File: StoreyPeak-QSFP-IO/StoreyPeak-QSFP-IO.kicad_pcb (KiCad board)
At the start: 2 copper layers, 30.1 x 69.8 mm, 26 parts, among them U1 QSFP_PCB-QSFP, U3 CH340G, X1 X322512MSB4SI

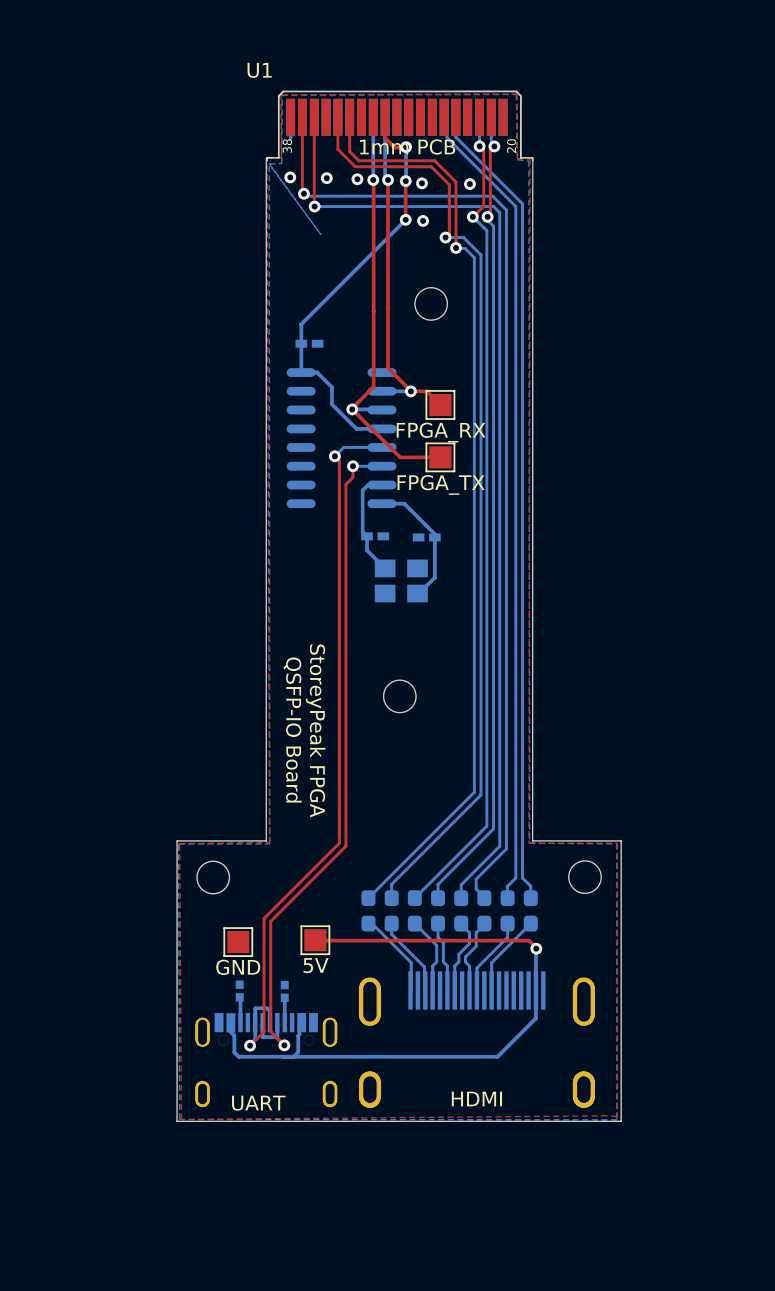
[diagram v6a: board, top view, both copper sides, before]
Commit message: Fix board outline cuts
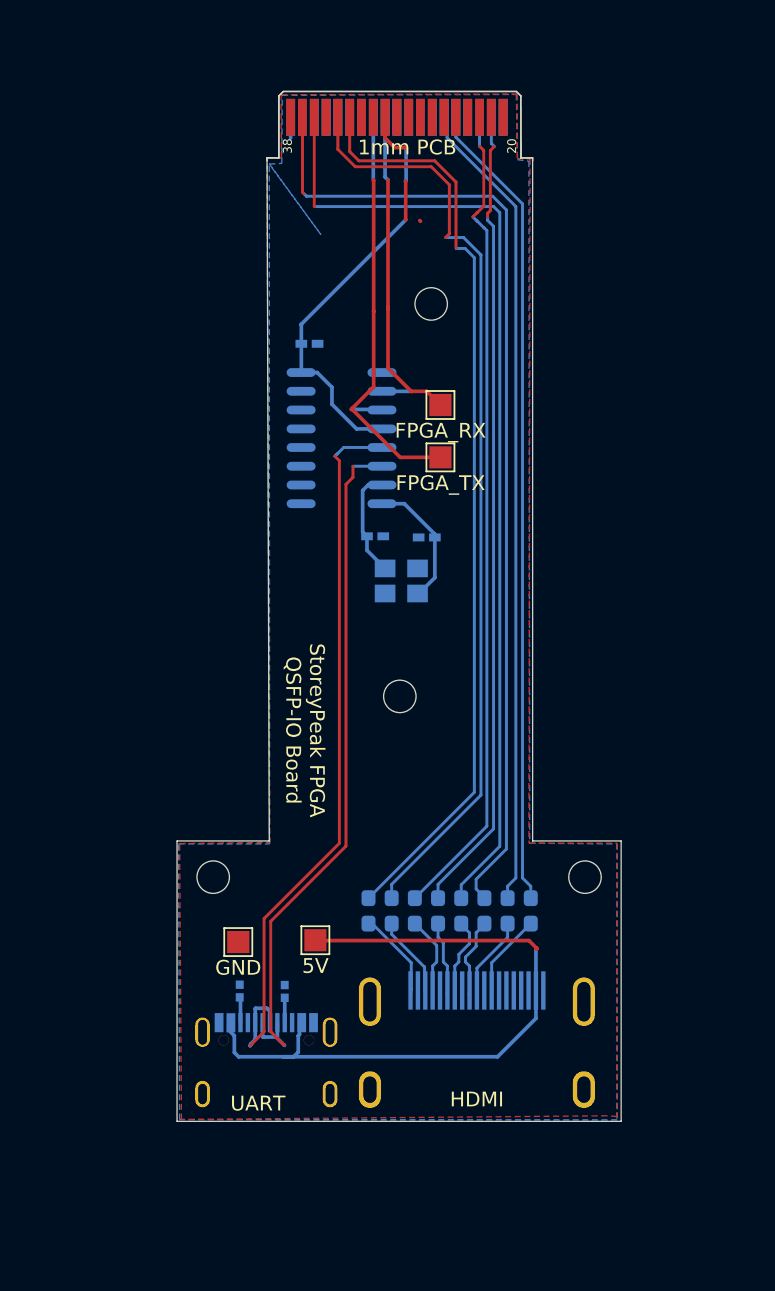
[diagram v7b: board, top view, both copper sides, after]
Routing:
- net Net-(U1-SDA): vias 2 -> 0
- net Net-(U1-SCL): vias 2 -> 0
- net GND: vias 6 -> 0
- net /USB_D-: vias 2 -> 0
- net /USB_D+: vias 2 -> 0
- net /QSFP_D2-: vias 1 -> 0
- net /QSFP_D2+: vias 1 -> 0
- net /QSFP_D1-: vias 2 -> 0
- net /QSFP_D1+: vias 2 -> 0
- net /QSFP_D0-: vias 1 -> 0
- net /QSFP_D0+: vias 1 -> 0
- net +5V: vias 1 -> 0
- net +3V3: vias 3 -> 0
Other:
- outline, holes or cut-outs redrawn

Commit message: Re-add vias (oops), add DP/DM pads, extend ground planes to cover entire board, stitch ground planes together
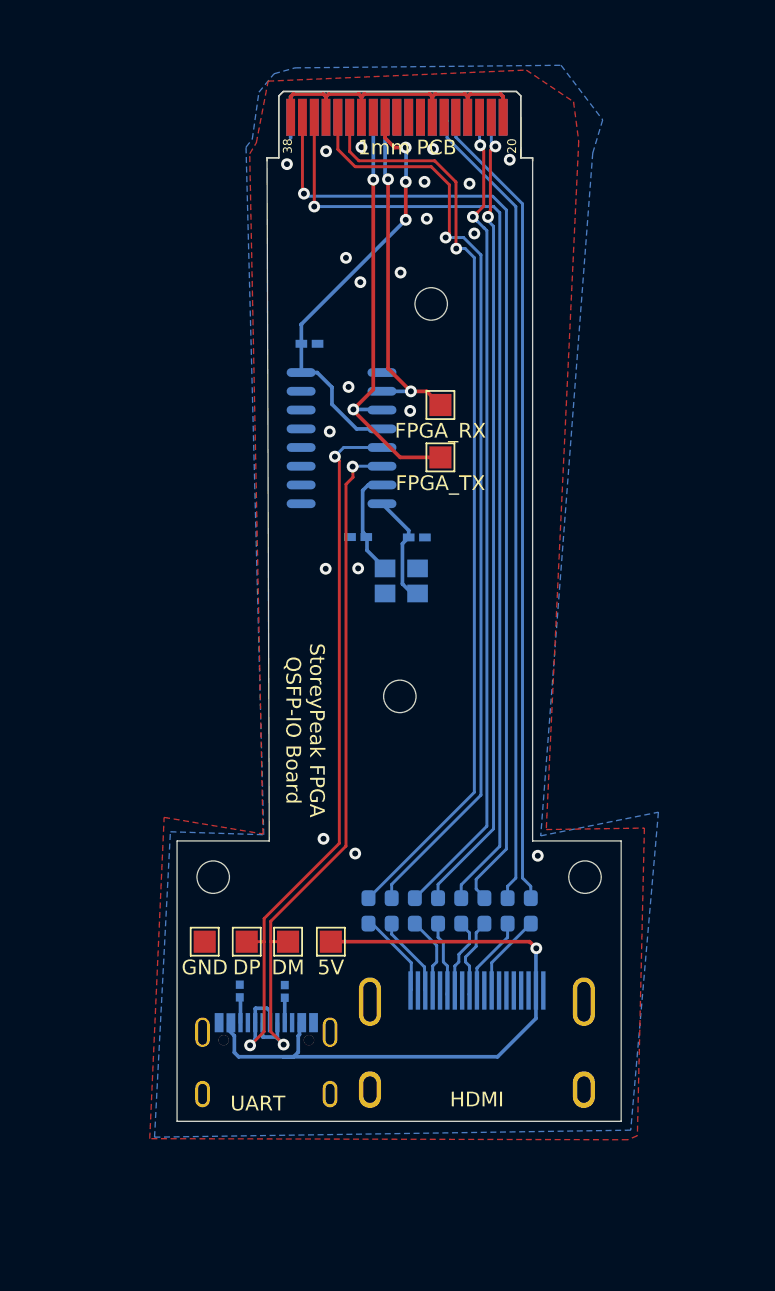
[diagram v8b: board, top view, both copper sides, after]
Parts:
- added TP5: DP, TestPoint:TestPoint_Pad_1.5x1.5mm, F.Cu at (151.6, 120.8)
- added TP6: DM, TestPoint:TestPoint_Pad_1.5x1.5mm, F.Cu at (154.4, 120.8)
- moved TP2 2.28 mm to (148.8, 120.8)
- moved C1 1.15 mm to (159.2, 93.4), turned to 0 degrees
- moved TP1 1.05 mm to (157.3, 120.8)
- moved C2 0.67 mm to (163.2, 93.4), turned to 180 degrees
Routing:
- net GND: track 1.67 -> 48.6 mm, vias 0 -> 20
- net Net-(U3-XO): track 9.00 -> 7.76 mm
- net /USB_D+: track 50.9 -> 52.1 mm, vias 0 -> 2
- net /USB_D-: track 47.7 -> 48.9 mm, vias 0 -> 2
- net +5V: track 46.9 -> 45.7 mm, vias 0 -> 1
- net /QSFP_D1-: track 54.9 -> 55.1 mm, vias 0 -> 2
- net Net-(U1-SDA): track 29.8 -> 29.9 mm, vias 0 -> 2
- net Net-(U1-SCL): vias 0 -> 2
- net /QSFP_D1+: track 55.7 -> 55.8 mm, vias 0 -> 2
- net /QSFP_D2+: vias 0 -> 1
- net /QSFP_D0+: vias 0 -> 1
- net /QSFP_D0-: vias 0 -> 1
- net +3V3: vias 0 -> 3
- net /QSFP_D2-: track 63.4 -> 63.5 mm, vias 0 -> 1
